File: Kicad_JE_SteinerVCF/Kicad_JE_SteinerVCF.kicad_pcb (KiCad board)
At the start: 2 copper layers, 100 x 100 mm, 98 parts, among them J101 AudioJack2_SwitchT, J102 AudioJack2_SwitchT, J103 AudioJack2_SwitchT, J104 AudioJack2_SwitchT, J105 AudioJack2_SwitchT, J201 HP, J202 BP, J203 LP, J204 Out, J205 CV, P101 Doepfer_Power_10pin, P201 Doepfer_Power_10pin, Q101 BC559, Q102 BC549, Q103 BC549, Q104 BC549, Q201 MMBT2907A, Q202 MMBT2222A, Q203 MMBT2222A, Q204 MMBT2222A

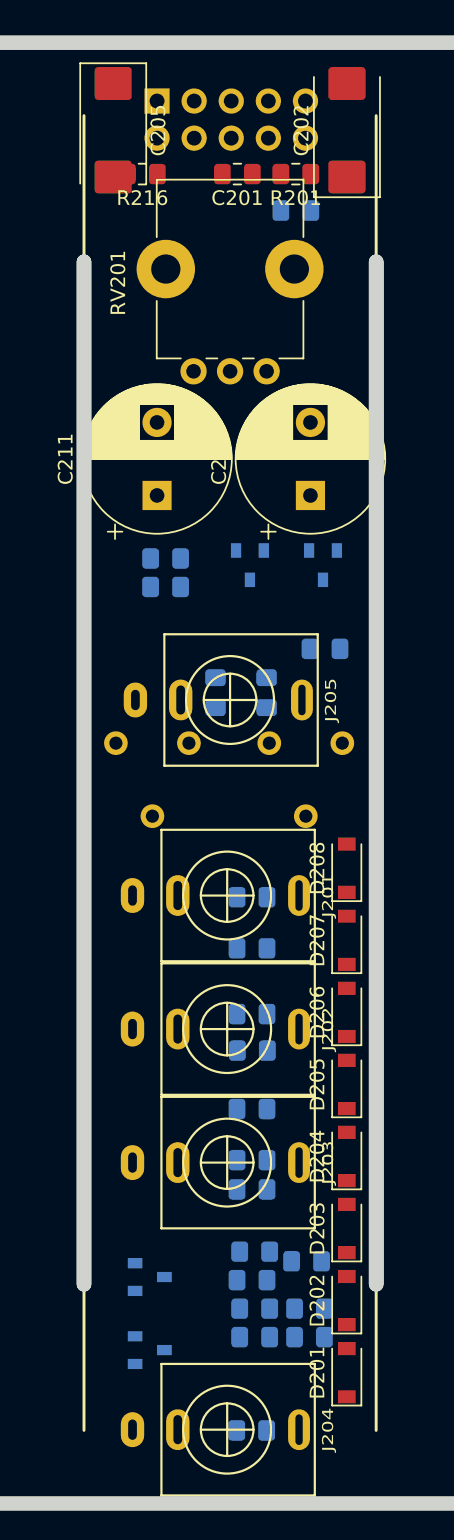
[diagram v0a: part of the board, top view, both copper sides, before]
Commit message: SMD section routed RevA
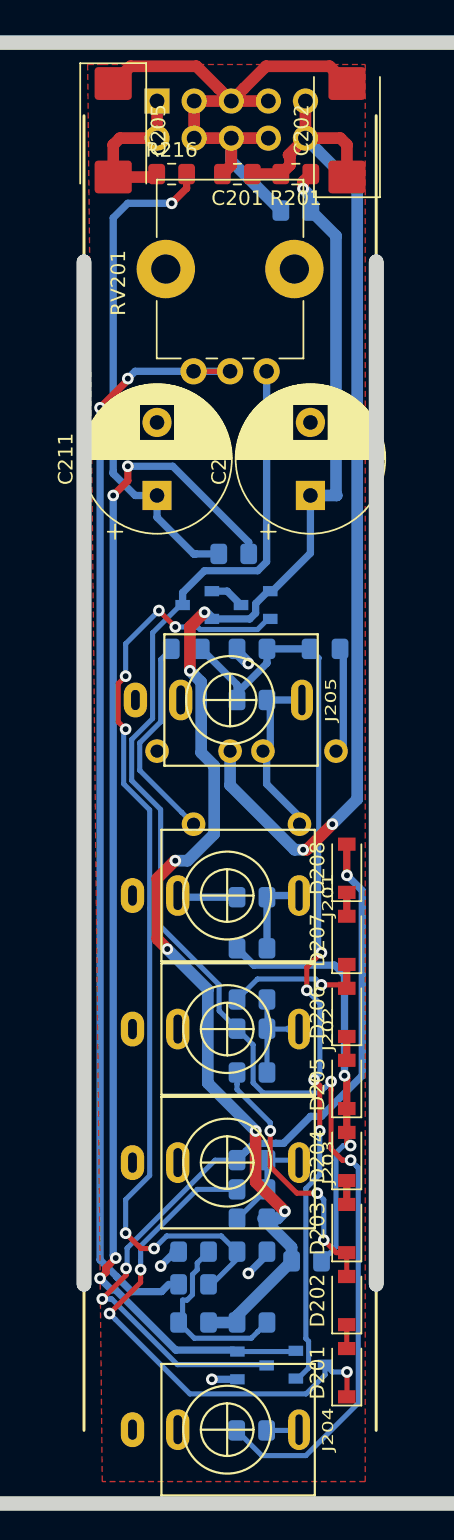
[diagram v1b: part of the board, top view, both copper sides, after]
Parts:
- moved R205 19.6 mm to (101.5, 117.5), turned to 180 degrees
- moved R211 12.5 mm to (106.5, 91.5)
- moved Q203 12.5 mm to (105.5, 140.5)
- moved RV202 10.1 mm to (107.2, 98.5)
- moved R215 9.50 mm to (97.0, 91.5), turned to 180 degrees
- moved RV203 7.70 mm to (100.0, 98.5)
- moved Q204 7.08 mm to (101.5, 140.6)
- moved R209 5.50 mm to (101.5, 128.5)
- moved Q202 5.36 mm to (101.8, 88.5), turned to 180 degrees
- moved R214 5.18 mm to (100.2, 85.0)
- moved Q201 4.52 mm to (97.8, 88.5), turned to 180 degrees
- moved R204 4.50 mm to (97.5, 135.0)
- moved R206 4.45 mm to (97.5, 132.8)
- moved R202 4.30 mm to (97.5, 137.6)
- moved R203 4.06 mm to (101.5, 137.6), turned to 180 degrees
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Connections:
- C206 pad 2: FilterOut -> FilterOut2
- C207 pad 2: Out -> Out2
- C208 pad 2: BP -> BP2
- C209 pad 1: FilterOut -> FilterOut2
- C209 pad 2: HP -> HP2
- C210 pad 2: BP -> BP2
- D204 pad 2: FilterOut -> FilterOut2
- D205 pad 1: FilterOut -> FilterOut2
- J201 pad T: HP -> HP2
- J202 pad T: BP -> BP2
- J203 pad T: LP -> LP2
- J204 pad T: Out -> Out2
- J205 pad T: CV -> CV2
- R205 pad 1: BP -> BP2
- R208 pad 1: LP -> LP2
- R209 pad 2: LP -> LP2
- R210 pad 2: LP -> LP2
- R212 pad 2: CV -> CV2
- R213 pad 2: HP -> HP2
- RV202 pad 2: CV -> CV2
- RV202 pad 3: CV -> CV2
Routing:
- net VCC: track 0.00 -> 99.2 mm, vias 0 -> 7
- net Net-(C207-Pad1): track 0.00 -> 97.8 mm, vias 0 -> 2
- net Net-(Q203-Pad2): track 0.00 -> 83.0 mm, vias 0 -> 4
- net Net-(R204-Pad1): track 0.00 -> 77.3 mm, vias 0 -> 2
- net +12VA: track 0.00 -> 74.0 mm, vias 0 -> 2
- net Net-(Q202-Pad2): track 0.00 -> 66.1 mm, vias 0 -> 6
- net Net-(Q203-Pad1): track 0.00 -> 64.1 mm, vias 0 -> 4
- net Net-(D208-Pad2): track 0.00 -> 54.3 mm, vias 0 -> 3
- net Net-(C211-Pad1): track 0.00 -> 53.9 mm, vias 0 -> 1
- net GNDA: track 0.00 -> 51.5 mm, vias 0 -> 4
- net Net-(D201-Pad1): track 0.00 -> 35.4 mm, vias 0 -> 3
- net FilterOut2: track 0.00 -> 29.1 mm, vias 0 -> 2
- net Net-(C208-Pad1): track 0.00 -> 18.5 mm, vias 0 -> 3
- net Net-(R215-Pad2): track 0.00 -> 14.4 mm
- net Net-(R202-Pad1): track 0.00 -> 12.8 mm
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- added copper zone on F.Cu, net GNDA
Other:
- net class Default: trace_width 0.25 -> 0.35
- net class Power added: clearance 0.2, trace_width 0.8, via_dia 0.8, via_drill 0.4

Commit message: THT Start - Label upd
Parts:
- C102, C103, C105, C107, C111, P101: moved to B.Cu
- moved P101 96.3 mm to (65.2, 53.8), turned to 270 degrees
- moved C105 87.7 mm to (77.8, 4.39)
- moved J102 82.4 mm to (60.2, 123.5)
- moved RV103 70.0 mm to (80.2, 108.5)
- moved C102 68.9 mm to (62.8, 4.39)
- moved RV101 59.3 mm to (80.2, 78.5)
- moved C103 59.2 mm to (62.8, 19.4)
- moved RV102 56.5 mm to (80.2, 93.5)
- moved C107 55.1 mm to (62.8, 34.4)
- moved C111 54.6 mm to (45.2, 38.5)
- moved J103 53.8 mm to (60.2, 68.5)
- moved J104 37.7 mm to (60.2, 93.5)
- moved J101 36.8 mm to (60.2, 78.5)
- moved J105 26.9 mm to (60.2, 108.5)
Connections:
- C103 pad 1: VCC -> +10V
- C104 pad 1: VCC -> +10V
- C106 pad 1: VCC -> +10V
- Q101 pad 1: VCC -> +10V
- Q102 pad 2: VCC -> +10V
- R101 pad 1: VCC -> +10V
- R102 pad 2: VCC -> +10V
- R103 pad 2: VCC -> +10V
- R108 pad 2: VCC -> +10V

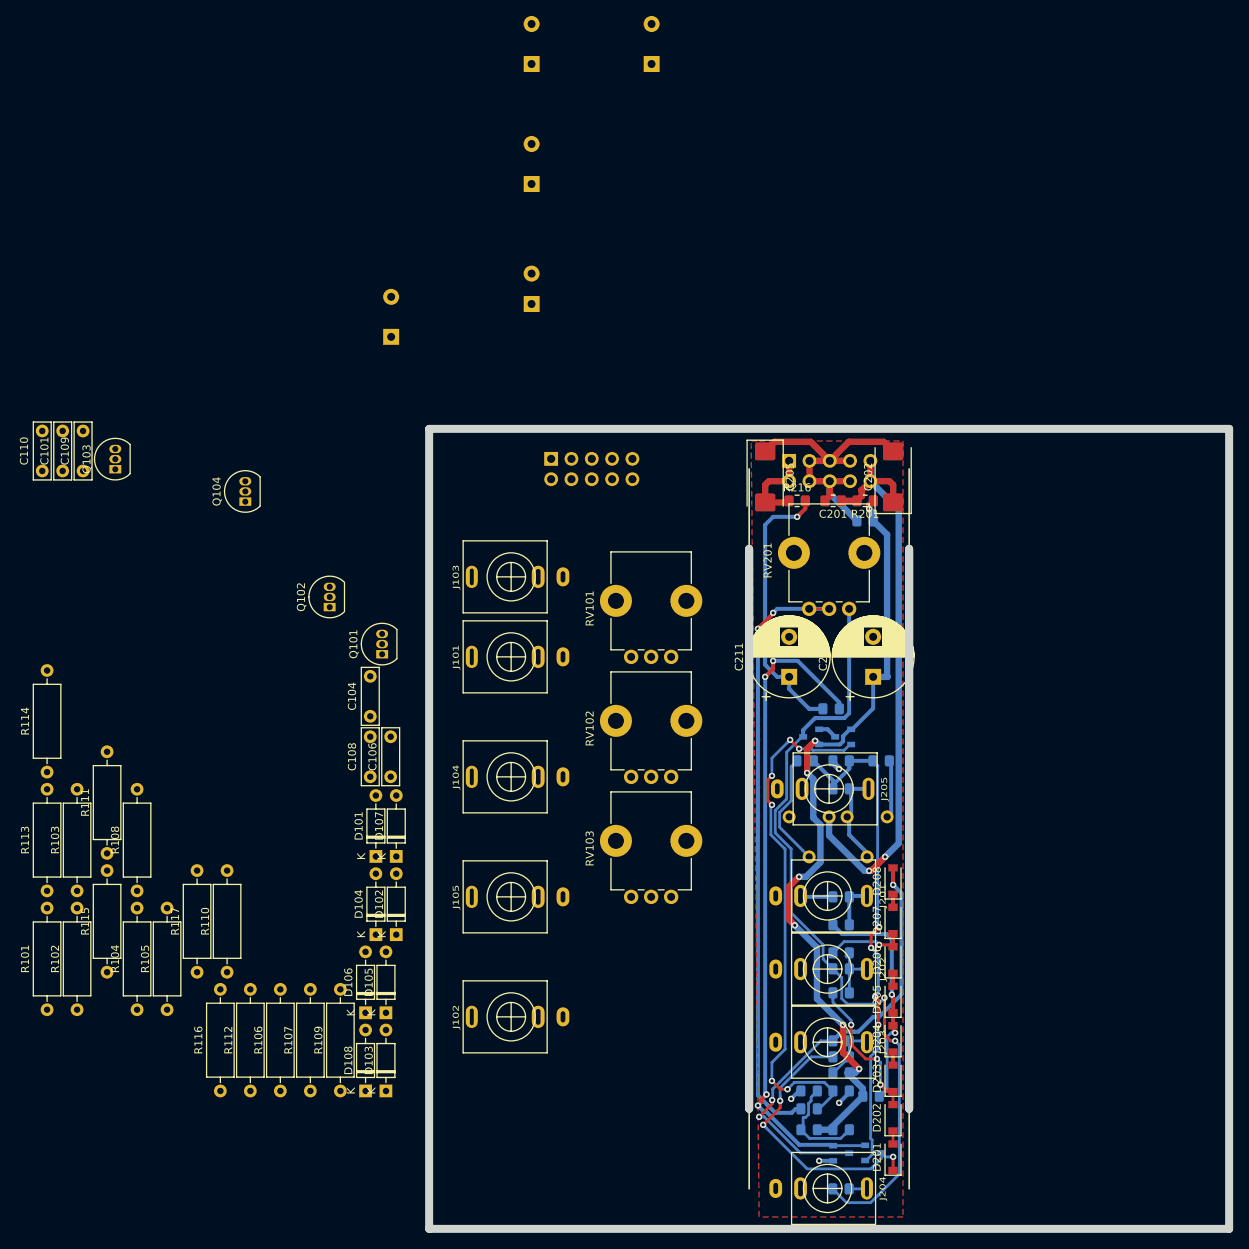
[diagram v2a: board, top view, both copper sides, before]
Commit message: THT complete placement - RevA
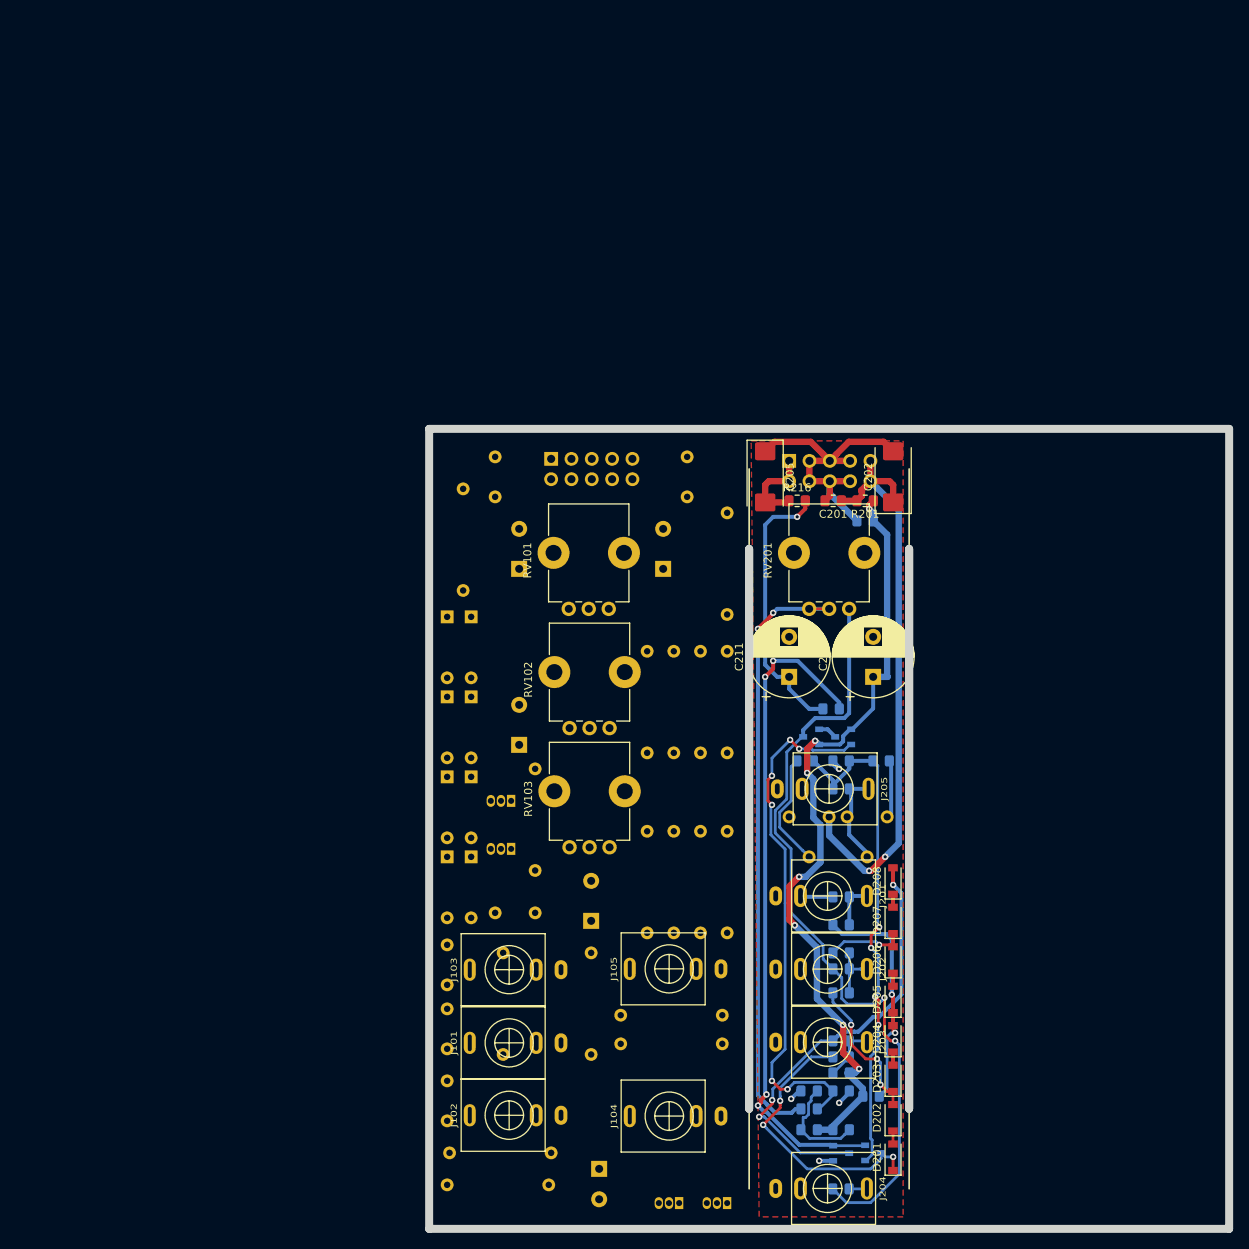
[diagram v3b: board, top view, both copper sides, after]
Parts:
- C101, C104, C106, C108, C109, C110, D101, D102, D103, D104, D105, D106, D107, D108, Q101, Q102, Q103, Q104, R101, R102, R103, R104, R105, R106, R107, R108, R109, R110, R111, R112, R113, R114, R115, R116, R117: moved to B.Cu
- J101: value AudioJack2_SwitchT -> HP
- J102: value AudioJack2_SwitchT -> BP
- J103: value AudioJack2_SwitchT -> LP
- J104: value AudioJack2_SwitchT -> Out
- J105: value AudioJack2_SwitchT -> CV
- moved C107 108.4 mm to (71.2, 142.5), turned to 270 degrees
- moved R101 105.3 mm to (87.2, 60.5), turned to 270 degrees
- moved C103 92.4 mm to (70.2, 111.5)
- moved Q102 89.5 mm to (87.2, 146.8), turned to 180 degrees
- moved R115 84.3 mm to (83.9, 77.8), turned to 270 degrees
- moved R103 81.4 mm to (87.2, 113.0)
- moved C109 81.2 mm to (52.2, 122.5), turned to 270 degrees
- moved R116 81.2 mm to (54.2, 57.5), turned to 270 degrees
- moved R112 81.1 mm to (87.2, 77.8), turned to 270 degrees
- moved C110 79.1 mm to (58.2, 110.5), turned to 0 degrees
- moved R102 78.5 mm to (83.9, 113.0)
- moved Q101 78.0 mm to (81.2, 146.8), turned to 180 degrees
- moved R117 71.8 mm to (80.6, 77.8), turned to 270 degrees
- moved R113 71.0 mm to (65.2, 140.5), turned to 180 degrees
- moved R111 68.7 mm to (77.2, 90.5)
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
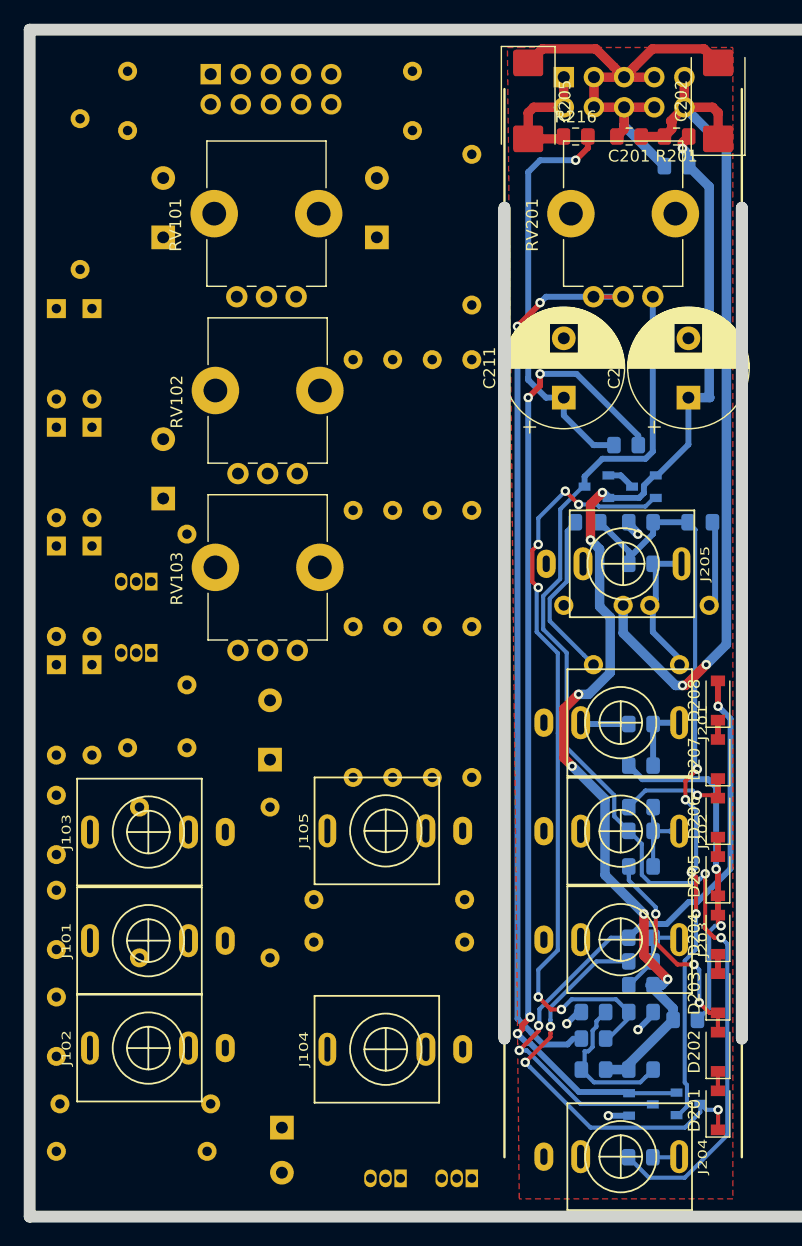
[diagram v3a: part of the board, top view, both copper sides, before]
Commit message: Connection Cleanup on both VCF
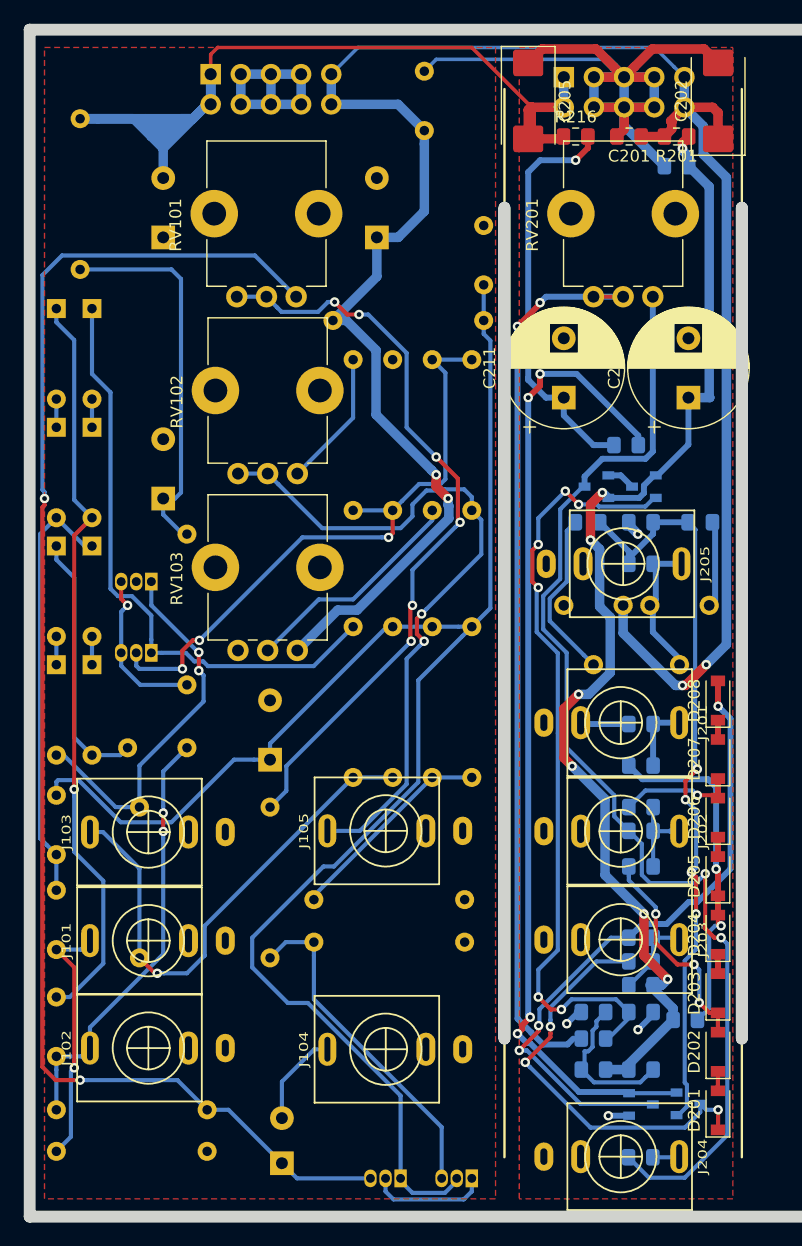
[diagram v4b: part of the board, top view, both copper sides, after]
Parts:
- moved C101 25.0 mm to (83.2, 58.5)
- moved C104 14.3 mm to (88.2, 71.5)
- moved R101 14.0 mm to (88.2, 74.5), turned to 180 degrees
- moved R113 4.01 mm to (65.0, 144.5)
- moved R105 3.50 mm to (52.2, 141.0)
- moved C107 3.00 mm to (71.2, 145.5), turned to 90 degrees
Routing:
- net +10V: track 0.00 -> 141.8 mm
- net Net-(C107-Pad1): track 0.00 -> 121.9 mm, vias 0 -> 2
- net +12VA: track 74.0 -> 176.0 mm, vias 2 -> 4
- net -12VA: track 11.0 -> 88.6 mm
- net Net-(R104-Pad1): track 0.00 -> 63.8 mm, vias 0 -> 6
- net Net-(C108-Pad1): track 0.00 -> 63.2 mm, vias 0 -> 1
- net CV: track 0.00 -> 59.8 mm, vias 0 -> 2
- net Net-(Q103-Pad2): track 0.00 -> 53.1 mm, vias 0 -> 3
- net GNDA: track 51.5 -> 102.4 mm
- net Net-(D101-Pad1): track 0.00 -> 50.6 mm
- net LP: track 0.00 -> 43.1 mm, vias 0 -> 1
- net FilterOut: track 0.00 -> 36.5 mm
- net BP: track 0.00 -> 36.3 mm, vias 0 -> 2
- net Net-(C111-Pad1): track 0.00 -> 32.6 mm
- net Net-(D108-Pad2): track 0.00 -> 31.9 mm, vias 0 -> 2
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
